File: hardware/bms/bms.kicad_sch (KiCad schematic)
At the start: 36 parts, among them J1 Screw_Terminal_01x01, J10 Conn_01x10, J11 USB_C_Receptacle_USB2.0, J12 Conn_01x03, J13 Conn_01x07, J2 Screw_Terminal_01x01, J3 Screw_Terminal_01x01, J4 Screw_Terminal_01x01, J5 Screw_Terminal_01x01, J6 Conn_01x02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

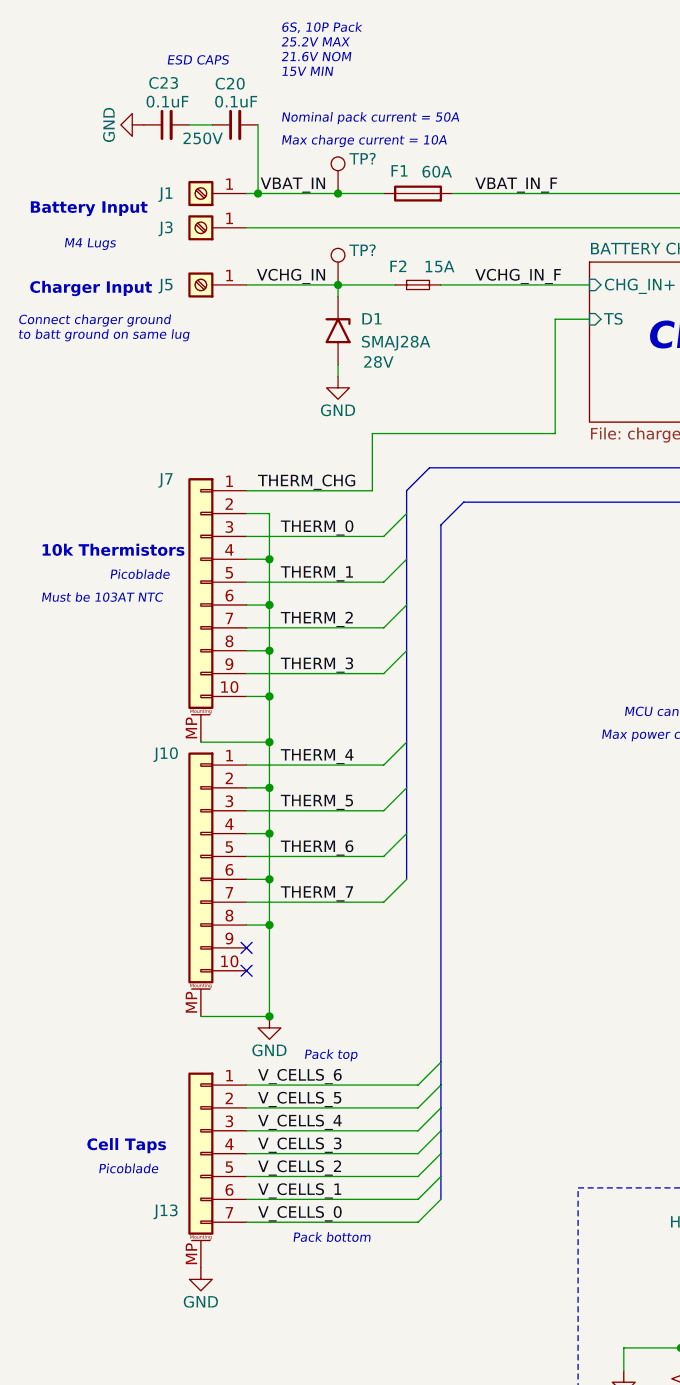
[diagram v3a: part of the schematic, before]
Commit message: Review of BMS board looks good, finished!
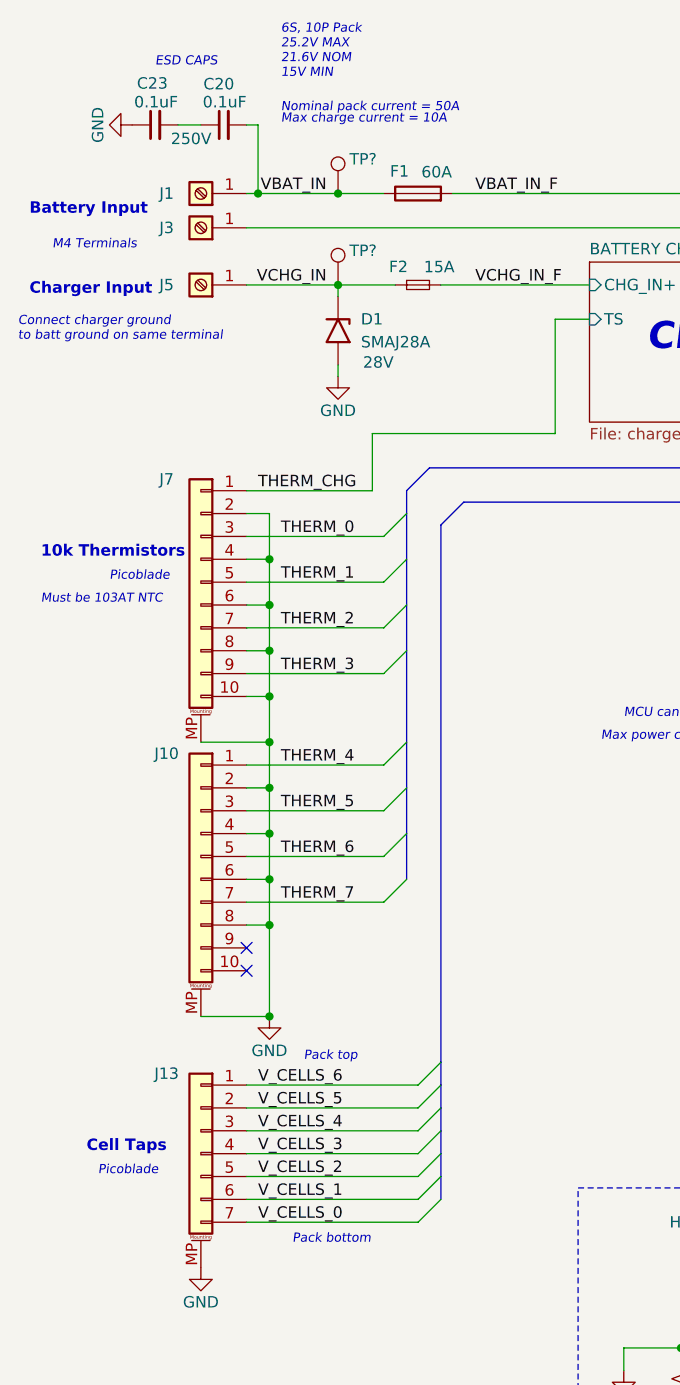
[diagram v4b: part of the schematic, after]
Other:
- note added: "Connect charger ground to batt ground on same terminal"
- note added: "M4 Terminals"
- note removed: "Connect charger ground to batt ground on same lug"
- moved on the sheet: C20, C23
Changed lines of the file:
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@@
   (junction (at 54.61 46.99) (diameter 0) (color 0 0 0 0)
   )
+  (junction (at 46.99 107.95) (diameter 0) (color 0 0 0 0)
+  )
+  (junction (at 266.7 157.48) (diameter 0) (color 0 0 0 0)
+  )
+  (junction (at 250.19 132.08) (diameter 0) (color 0 0 0 0)
+  )
+  (junction (at 46.99 97.79) (diameter 0) (color 0 0 0 0)
+  )
+  (junction (at 205.74 73.66) (diameter 0) (color 0 0 0 0)
+  )
+  (junction (at 100.33 172.72) (diameter 0) (color 0 0 0 0)
+  )
+  (junction (at 46.99 87.63) (diameter 0) (color 0 0 0 0)
+  )
+  (junction (at 238.76 124.46) (diameter 0) (color 0 0 0 0)
+  )
+  (junction (at 46.99 102.87) (diameter 0) (color 0 0 0 0)
+  )
+  (junction (at 46.99 113.03) (diameter 0) (color 0 0 0 0)
+  )
+  (junction (at 92.71 172.72) (diameter 0) (color 0 0 0 0)
+  )
   (junction (at 45.72 36.83) (diameter 0) (color 0 0 0 0)
-  )
-  (junction (at 46.99 107.95) (diameter 0) (color 0 0 0 0)
-  )
-  (junction (at 266.7 157.48) (diameter 0) (color 0 0 0 0)
-  )
-  (junction (at 250.19 132.08) (diameter 0) (color 0 0 0 0)
-  )
-  (junction (at 46.99 97.79) (diameter 0) (color 0 0 0 0)
-  )
-  (junction (at 205.74 73.66) (diameter 0) (color 0 0 0 0)
-  )
-  (junction (at 100.33 172.72) (diameter 0) (color 0 0 0 0)
-  )
-  (junction (at 46.99 87.63) (diameter 0) (color 0 0 0 0)
-  )
-  (junction (at 238.76 124.46) (diameter 0) (color 0 0 0 0)
-  )
-  (junction (at 46.99 102.87) (diameter 0) (color 0 0 0 0)
-  )
-  (junction (at 46.99 113.03) (diameter 0) (color 0 0 0 0)
-  )
-  (junction (at 92.71 172.72) (diameter 0) (color 0 0 0 0)
   )
   (junction (at 250.19 137.16) (diameter 0) (color 0 0 0 0)
@@
     (stroke (width 0) (type default))
   )
-  (wire (pts (xy 45.72 36.83) (xy 54.61 36.83))
-    (stroke (width 0) (type default))
-  )
   (bus (pts (xy 66.04 135.89) (xy 66.04 138.43))
     (stroke (width 0) (type default))
@@
     (stroke (width 0) (type default))
   )
+  (wire (pts (xy 45.72 29.21) (xy 44.45 29.21))
+    (stroke (width 0) (type default))
+  )
   (wire (pts (xy 46.99 118.11) (xy 46.99 128.27))
     (stroke (width 0) (type default))
@@
   )
   (wire (pts (xy 46.99 97.79) (xy 46.99 102.87))
+    (stroke (width 0) (type default))
+  )
+  (wire (pts (xy 45.72 36.83) (xy 44.45 36.83))
     (stroke (width 0) (type default))
   )
@@
     (stroke (width 0) (type dash))
   )
+  (wire (pts (xy 45.72 36.83) (xy 54.61 36.83))
+    (stroke (width 0) (type default))
+  )
   (wire (pts (xy 121.92 114.3) (xy 125.73 114.3))
     (stroke (width 0) (type default))
@@
     (stroke (width 0) (type default))
   )
-  (wire (pts (xy 40.64 29.21) (xy 38.1 29.21))
+  (wire (pts (xy 39.37 29.21) (xy 36.83 29.21))
     (stroke (width 0) (type default))
   )
@@
     (stroke (width 0) (type default))
   )
-  (wire (pts (xy 44.45 36.83) (xy 45.72 36.83))
-    (stroke (width 0) (type default))
-  )
   (wire (pts (xy 208.28 76.2) (xy 227.33 76.2))
     (stroke (width 0) (type default))
@@
     (stroke (width 0) (type dash))
   )
-  (text "Connect charger ground \nto batt ground on same lug"
+  (text "Connect charger ground \nto batt ground on same terminal"
     (at 19.05 53.34 0)
     (effects (font (size 1.016 1.016) italic) (justify left bottom))
@@
     (effects (font (size 1.016 1.016) italic) (justify left bottom))
   )
-  (text "Max charge current = 10A" (at 48.26 31.75 0)
+  (text "Max charge current = 10A" (at 48.26 29.21 0)
     (effects (font (size 1.016 1.016) italic) (justify left bottom))
   )
@@
     (effects (font (size 1.27 1.27) (thickness 0.254) bold) (justify left bottom))
   )
-  (text "Nominal pack current = 50A" (at 48.26 29.21 0)
+  (text "Nominal pack current = 50A" (at 48.26 27.94 0)
     (effects (font (size 1.016 1.016) italic) (justify left bottom))
   )
@@
     (effects (font (size 1.016 1.016) italic) (justify left bottom))
   )
-  (text "ESD CAPS" (at 35.56 22.86 0)
+  (text "ESD CAPS" (at 34.29 22.86 0)
     (effects (font (size 1.016 1.016) italic) (justify left bottom))
   )
@@
     (effects (font (size 1.016 1.016) italic) (justify left bottom))
   )
-  (text "M4 Lugs" (at 24.13 43.18 0)
+  (text "M4 Terminals" (at 22.86 43.18 0)
     (effects (font (size 1.016 1.016) italic) (justify left bottom))
   )
@@
   (symbol (lib_id "Connector_Generic_MountingPin:Conn_01x07_MountingPin") (at 39.37 143.51 0) (mirror y) (unit 1)
     (in_bom yes) (on_board yes) (dnp no)
-    (property "Reference" "J13" (at 35.56 149.86 0)
+    (property "Reference" "J13" (at 35.56 134.62 0)
       (effects (font (size 1.27 1.27)))
     )
@@
     )
   )
-  (symbol (lib_id "Device:C_Small") (at 43.18 29.21 90) (unit 1)
-    (in_bom yes) (on_board yes) (dnp no)
-    (property "Reference" "C20" (at 44.3515 24.6695 90)
-      (effects (font (size 1.27 1.27)) (justify left))
-    )
-    (property "Value" "0.1uF" (at 45.72 26.67 90)
-      (effects (font (size 1.27 1.27)) (justify left))
-    )
-    (property "Footprint" "Capacitor_SMD:C_0805_2012Metric" (at 43.18 29.21 0)
-      (effects (font (size 1.27 1.27)) hide)
-    )
-    (property "Datasheet" "~" (at 43.18 29.21 0)
-      (effects (font (size 1.27 1.27)) hide)
-    )
-    (property "MFG" "TDK Corporation" (at 43.18 29.21 0)
-      (effects (font (size 1.27 1.27)) hide)
-    )
-    (property "MFG PN" "CGA4J3X7T2E104K125AA" (at 43.18 29.21 0)
-      (effects (font (size 1.27 1.27)) hide)
-    )
-    (property "Voltage" "250V" (at 45.4914 26.8732 0)
+  (symbol (lib_id "Device:C_Small") (at 41.91 29.21 90) (unit 1)
+    (in_bom yes) (on_board yes) (dnp no)
+    (property "Reference" "C20" (at 43.0815 24.6695 90)
+      (effects (font (size 1.27 1.27)) (justify left))
+    )
+    (property "Value" "0.1uF" (at 44.45 26.67 90)
+      (effects (font (size 1.27 1.27)) (justify left))
+    )
+    (property "Footprint" "Capacitor_SMD:C_0805_2012Metric" (at 41.91 29.21 0)
+      (effects (font (size 1.27 1.27)) hide)
+    )
+    (property "Datasheet" "~" (at 41.91 29.21 0)
+      (effects (font (size 1.27 1.27)) hide)
+    )
+    (property "MFG" "TDK Corporation" (at 41.91 29.21 0)
+      (effects (font (size 1.27 1.27)) hide)
+    )
+    (property "MFG PN" "CGA4J3X7T2E104K125AA" (at 41.91 29.21 0)
+      (effects (font (size 1.27 1.27)) hide)
+    )
+    (property "Voltage" "250V" (at 44.2214 26.8732 0)
       (effects (font (size 1.27 1.27)) (justify left) hide)
     )
@@
     )
   )
-  (symbol (lib_id "power:GND") (at 33.02 29.21 270) (unit 1)
-    (in_bom yes) (on_board yes) (dnp no)
-    (property "Reference" "#PWR080" (at 26.67 29.21 0)
-      (effects (font (size 1.27 1.27)) hide)
-    )
-    (property "Value" "GND" (at 29.21 29.21 0)
-      (effects (font (size 1.27 1.27)))
-    )
-    (property "Footprint" "" (at 33.02 29.21 0)
-      (effects (font (size 1.27 1.27)) hide)
-    )
-    (property "Datasheet" "" (at 33.02 29.21 0)
+  (symbol (lib_id "power:GND") (at 31.75 29.21 270) (unit 1)
+    (in_bom yes) (on_board yes) (dnp no)
+    (property "Reference" "#PWR080" (at 25.4 29.21 0)
+      (effects (font (size 1.27 1.27)) hide)
+    )
+    (property "Value" "GND" (at 27.94 29.21 0)
+      (effects (font (size 1.27 1.27)))
+    )
+    (property "Footprint" "" (at 31.75 29.21 0)
+      (effects (font (size 1.27 1.27)) hide)
+    )
+    (property "Datasheet" "" (at 31.75 29.21 0)
       (effects (font (size 1.27 1.27)) hide)
     )
@@
     )
   )
-  (symbol (lib_id "Device:C_Small") (at 35.56 29.21 90) (unit 1)
-    (in_bom yes) (on_board yes) (dnp no)
-    (property "Reference" "C23" (at 36.9681 24.5905 90)
-      (effects (font (size 1.27 1.27)) (justify left))
-    )
-    (property "Value" "0.1uF" (at 38.1 26.67 90)
-      (effects (font (size 1.27 1.27)) (justify left))
-    )
-    (property "Footprint" "Capacitor_SMD:C_0805_2012Metric" (at 35.56 29.21 0)
-      (effects (font (size 1.27 1.27)) hide)
-    )
-    (property "Datasheet" "~" (at 35.56 29.21 0)
-      (effects (font (size 1.27 1.27)) hide)
-    )
-    (property "MFG" "TDK Corporation" (at 35.56 29.21 0)
-      (effects (font (size 1.27 1.27)) hide)
-    )
-    (property "MFG PN" "CGA4J3X7T2E104K125AA" (at 35.56 29.21 0)
-      (effects (font (size 1.27 1.27)) hide)
-    )
-    (property "Voltage" "250V" (at 41.8246 30.7499 90)
-      (effects (font (size 1.27 1.27)) (justify left))
-    )
+  (symbol (lib_id "Device:C_Small") (at 34.29 29.21 90) (unit 1)
+    (in_bom yes) (on_board yes) (dnp no)
+    (property "Reference" "C23" (at 35.6981 24.5905 90)
+      (effects (font (size 1.27 1.27)) (justify left))
+    )
+    (property "Value" "0.1uF" (at 36.83 26.67 90)
+      (effects (font (size 1.27 1.27)) (justify left))
+    )
+    (property "Footprint" "Capacitor_SMD:C_0805_2012Metric" (at 34.29 29.21 0)
+      (effects (font (size 1.27 1.27)) hide)
+    )
+    (property "Datasheet" "~" (at 34.29 29.21 0)
+      (effects (font (size 1.27 1.27)) hide)
+    )
+    (property "MFG" "TDK Corporation" (at 34.29 29.21 0)
+      (effects (font (size 1.27 1.27)) hide)
+    )
+    (property "MFG PN" "CGA4J3X7T2E104K125AA" (at 34.29 29.21 0)
+      (effects (font (size 1.27 1.27)) hide)
+    )
+    (property "Voltage" "250V" (at 40.5546 30.7499 90)
+      (effects (font (size 1.27 1.27)) (justify left))
+    )

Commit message: Finished battery holder board!
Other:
- note removed: "M4 Lugs"
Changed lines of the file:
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@@
     (effects (font (size 1.27 1.27) (thickness 0.254) bold) (justify left bottom))
   )
-  (text "M4 Lugs" (at 265.43 41.91 0)
+  (text "M4 Terminals" (at 265.43 41.91 0)
     (effects (font (size 1.016 1.016) italic) (justify left bottom))
   )

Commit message: Updated MFG PNs, BOM ordered.
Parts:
- H1, H2, H3, H4: now left out of the parts list
- SW?: MFG PN DIP SWITCH, SPST, 2.54 PITCH, FL -> DS04-254-2-01BK-SMT
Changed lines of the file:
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@@
   )
   (symbol (lib_id "Mechanical:MountingHole_Pad") (at 96.52 152.4 0) (unit 1)
-    (in_bom yes) (on_board yes) (dnp no)
+    (in_bom no) (on_board yes) (dnp no)
     (property "Reference" "H1" (at 91.44 151.13 0)
       (effects (font (size 1.27 1.27)) (justify left))
@@
   )
   (symbol (lib_id "Mechanical:MountingHole_Pad") (at 106.68 152.4 0) (unit 1)
-    (in_bom yes) (on_board yes) (dnp no)
+    (in_bom no) (on_board yes) (dnp no)
     (property "Reference" "H2" (at 101.6 151.13 0)
       (effects (font (size 1.27 1.27)) (justify left))
@@
   )
   (symbol (lib_id "Mechanical:MountingHole_Pad") (at 116.84 152.4 0) (unit 1)
-    (in_bom yes) (on_board yes) (dnp no)
+    (in_bom no) (on_board yes) (dnp no)
     (property "Reference" "H3" (at 111.76 151.13 0)
       (effects (font (size 1.27 1.27)) (justify left))
@@
   )
   (symbol (lib_id "Mechanical:MountingHole_Pad") (at 127 152.4 0) (unit 1)
-    (in_bom yes) (on_board yes) (dnp no)
+    (in_bom no) (on_board yes) (dnp no)
     (property "Reference" "H4" (at 121.92 151.13 0)
       (effects (font (size 1.27 1.27)) (justify left))
@@
       (effects (font (size 1.27 1.27)) hide)
     )
-    (property "MFG PN" "DIP SWITCH, SPST, 2.54 PITCH, FL" (at 240.03 64.77 90)
-      (effects (font (size 1.27 1.27)) hide)
-    )
+    (property "MFG PN" "DS04-254-2-01BK-SMT" (at 240.03 64.77 90)
+      (effects (font (size 1.27 1.27)) hide)
+    )
